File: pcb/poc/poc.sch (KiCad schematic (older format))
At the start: 57 parts, among them J1 USB_B_Mini, J2 Right, J3 Left, J4 AVR-ISP-6, J5 Conn_02x08_Odd_Even, J6 Conn_02x06_Odd_Even, SW1 SW_Push, SW2 SW_Push_45deg, SW3 SW_Push_45deg, SW4 SW_Push_45deg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

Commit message: pcb: poc: Assign footprints
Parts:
- added SW10, SW11: SW_Push_45deg, Button_Switch_Keyboard:SW_Cherry_MX_1.00u_PCB, symbol Switch:SW_Push_45deg
- C1: footprint (none) -> Capacitor_Tantalum_SMD:CP_EIA-3216-18_Kemet-A_Pad1.58x1.35mm_HandSolder
- C2, C3, C4, C5, C6, C7, C8, C9: footprint (none) -> Capacitor_SMD:C_0805_2012Metric_Pad1.18x1.45mm_HandSolder
- D10, D4: footprint (none) -> LED_SMD:LED_0805_2012Metric_Pad1.15x1.40mm_HandSolder
- D11, D12, D13, D14, D2, D6, D7, D8, D9: footprint (none) -> Diode_SMD:D_SOD-123
- F1: footprint (none) -> Fuse:Fuse_0805_2012Metric_Pad1.15x1.40mm_HandSolder
- J5: footprint (none) -> Connector_PinHeader_2.54mm:PinHeader_2x08_P2.54mm_Vertical
- J6: footprint (none) -> Connector_PinHeader_2.54mm:PinHeader_2x06_P2.54mm_Vertical
- R1, R10, R11, R12, R13, R14, R15, R2, R3, R4, R5, R6, R7, R8, R9: footprint (none) -> Resistor_SMD:R_0805_2012Metric_Pad1.20x1.40mm_HandSolder
- SW1, SW2, SW3, SW4, SW5, SW6, SW7, SW8, SW9: footprint (none) -> Button_Switch_THT:SW_PUSH_6mm_H4.3mm
- Y1: footprint (none) -> Crystal:Crystal_HC49-U_Vertical
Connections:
- net COL1: now also SW10.1
- net COL4: now also SW11.1
- net at D8.2 (A), SW4.2: now also SW10.2
- net at D13.2 (A), SW8.2: now also SW11.2

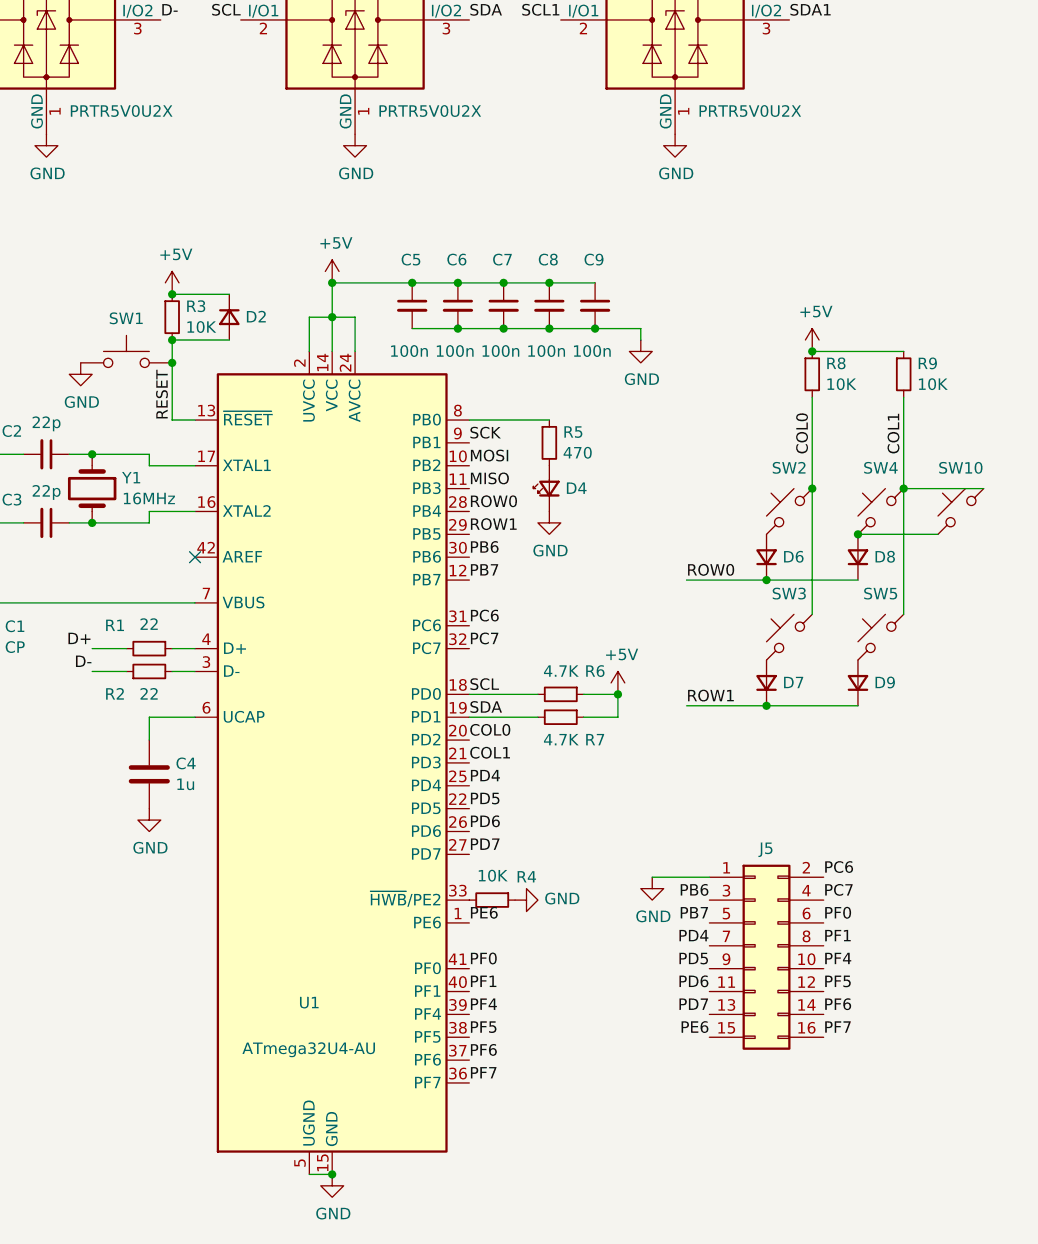
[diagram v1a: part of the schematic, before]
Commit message: pcb: poc: Some routing
Signed-off-by: Nikita Leshenko <nikita@leshenko.net>
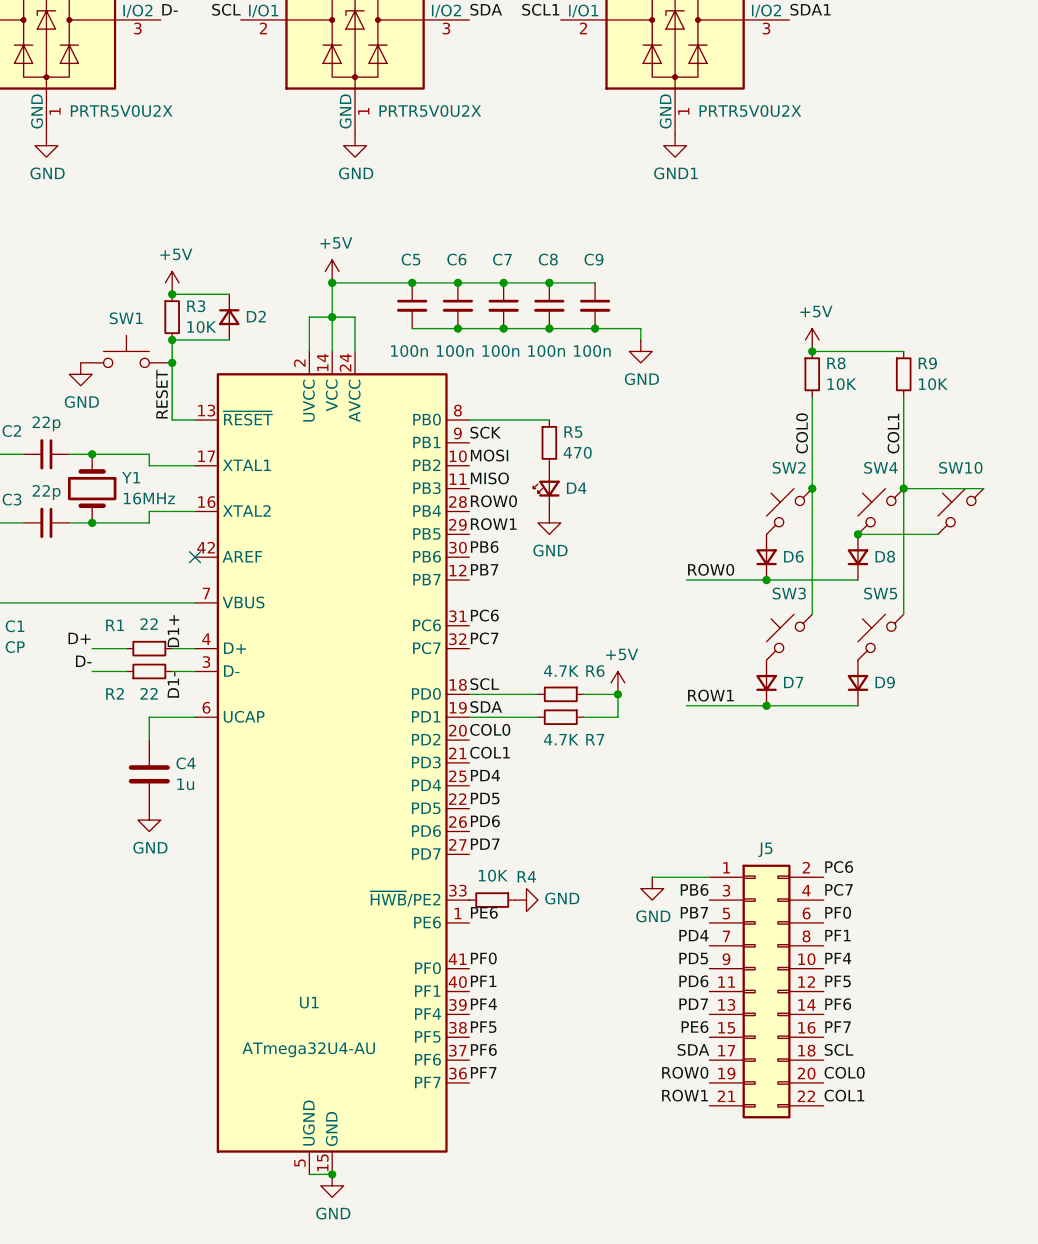
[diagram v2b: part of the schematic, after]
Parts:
- removed J5: Conn_02x08_Odd_Even, Connector_PinHeader_2.54mm:PinHeader_2x08_P2.54mm_Vertical, symbol Connector_Generic:Conn_02x08_Odd_Even
- added J5: Conn_02x11_Odd_Even, Connector_PinSocket_2.54mm:PinSocket_2x11_P2.54mm_Vertical, symbol Connector_Generic:Conn_02x11_Odd_Even
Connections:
- net COL0: now also J5.20 (Pin_20)
- net COL1: now also J5.22 (Pin_22)
- net GND: now also J5.1 (Pin_1); no longer D5.1 (GND)
- net GND1: now also D5.1 (GND)
- net PB6: now also J5.3 (Pin_3)
- net PB7: now also J5.5 (Pin_5)
- net PC6: now also J5.2 (Pin_2)
- net PC7: now also J5.4 (Pin_4)
- net PD4: now also J5.7 (Pin_7)
- net PD5: now also J5.9 (Pin_9)
- net PD6: now also J5.11 (Pin_11)
- net PD7: now also J5.13 (Pin_13)
- net PE6: now also J5.15 (Pin_15)
- net PF0: now also J5.6 (Pin_6)
- net PF1: now also J5.8 (Pin_8)
- net PF4: now also J5.10 (Pin_10)
- net PF5: now also J5.12 (Pin_12)
- net PF6: now also J5.14 (Pin_14)
- net PF7: now also J5.16 (Pin_16)
- net ROW0: now also J5.19 (Pin_19)
- net ROW1: now also J5.21 (Pin_21)
- net SCL: now also J5.18 (Pin_18)
- net SDA: now also J5.17 (Pin_17)
- net D1-: now reaches R2.2, U1.3 (D-)
- net D1+: now reaches R1.1, U1.4 (D+)
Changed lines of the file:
@@
-	1    0    0    -1
-$EndComp
-$Comp
-L power:GND #PWR027
-U 1 1 606CC318
-P 5150 1750
-F 0 "#PWR027" H 5150 1500 50  0001 C CNN
-F 1 "GND" H 5155 1577 50  0000 C CNN
-F 2 "" H 5150 1750 50  0001 C CNN
-F 3 "" H 5150 1750 50  0001 C CNN
-	1    5150 1750
 	1    0    0    -1
 $EndComp
@@
 Text Label 8650 4500 0    50   ~ 0
 COL4
-$Comp
-L Connector_Generic:Conn_02x08_Odd_Even J5
-U 1 1 60747A12
-P 5500 5300
-F 0 "J5" H 5550 5725 50  0000 C CNN
-F 1 "Conn_02x08_Odd_Even" H 5550 5726 50  0001 C CNN
-F 2 "Connector_PinHeader_2.54mm:PinHeader_2x08_P2.54mm_Vertical" H 5500 5300 50  0001 C CNN
-F 3 "~" H 5500 5300 50  0001 C CNN
-	1    5500 5300
-	1    0    0    -1
-$EndComp
 $Comp
 L Connector_Generic:Conn_02x06_Odd_Even J6
@@
 	10400 3500 10100 3500
 Connection ~ 10100 3500
+$Comp
+L power:GND1 #PWR0101
+U 1 1 604E5D44
+P 5150 1750
+F 0 "#PWR0101" H 5150 1500 50  0001 C CNN
+F 1 "GND1" H 5155 1577 50  0000 C CNN
+F 2 "" H 5150 1750 50  0001 C CNN
+F 3 "" H 5150 1750 50  0001 C CNN
+	1    5150 1750
+	1    0    0    -1
+$EndComp
+Text Label 5800 5800 0    50   ~ 0
+SCL
+Text Label 5300 5800 2    50   ~ 0
+SDA
+Text Label 5800 5900 0    50   ~ 0
+COL0
+Text Label 5800 6000 0    50   ~ 0
+COL1
+Text Label 5300 5900 2    50   ~ 0
+ROW0
+Text Label 5300 6000 2    50   ~ 0
+ROW1
+$Comp
+L Connector_Generic:Conn_02x11_Odd_Even J5
+U 1 1 604C9372
+P 5500 5500
+F 0 "J5" H 5550 6125 50  0000 C CNN
+F 1 "Conn_02x11_Odd_Even" H 5550 6126 50  0001 C CNN
+F 2 "Connector_PinSocket_2.54mm:PinSocket_2x11_P2.54mm_Vertical" H 5500 5500 50  0001 C CNN
+F 3 "~" H 5500 5500 50  0001 C CNN
+	1    5500 5500
+	1    0    0    -1
+$EndComp
+Text Label 3000 4000 1    50   ~ 0
+D1+
+Text Label 3000 4100 3    50   ~ 0
+D1-
 $EndSCHEMATC

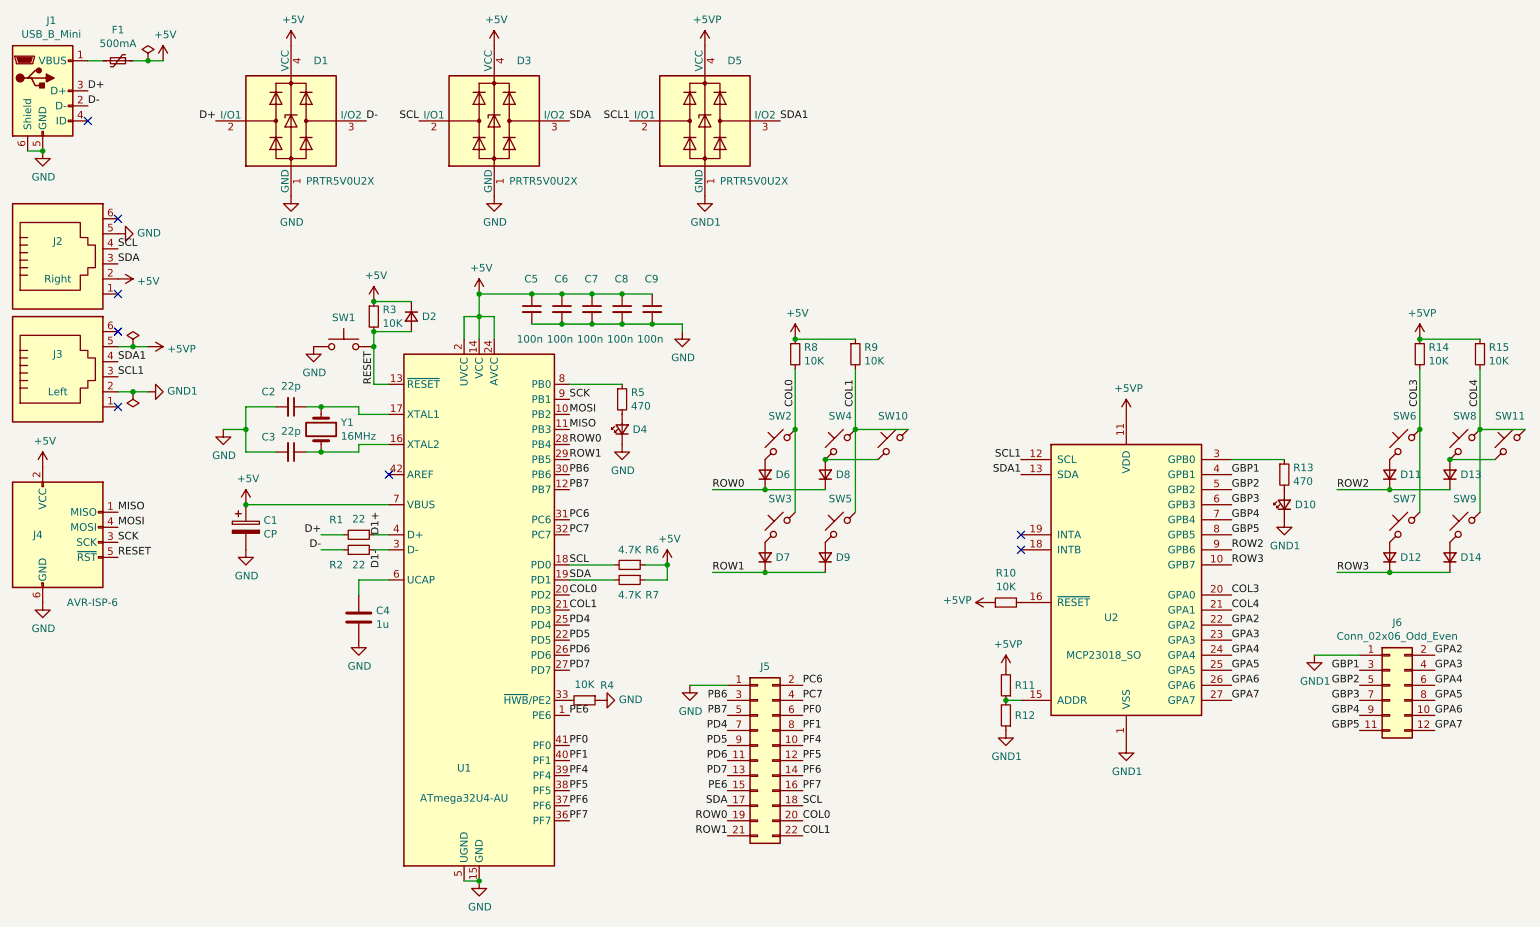
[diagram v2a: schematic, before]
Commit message: pcb: poc: Routed nabaz stuff
Signed-off-by: Nikita Leshenko <nikita@leshenko.net>
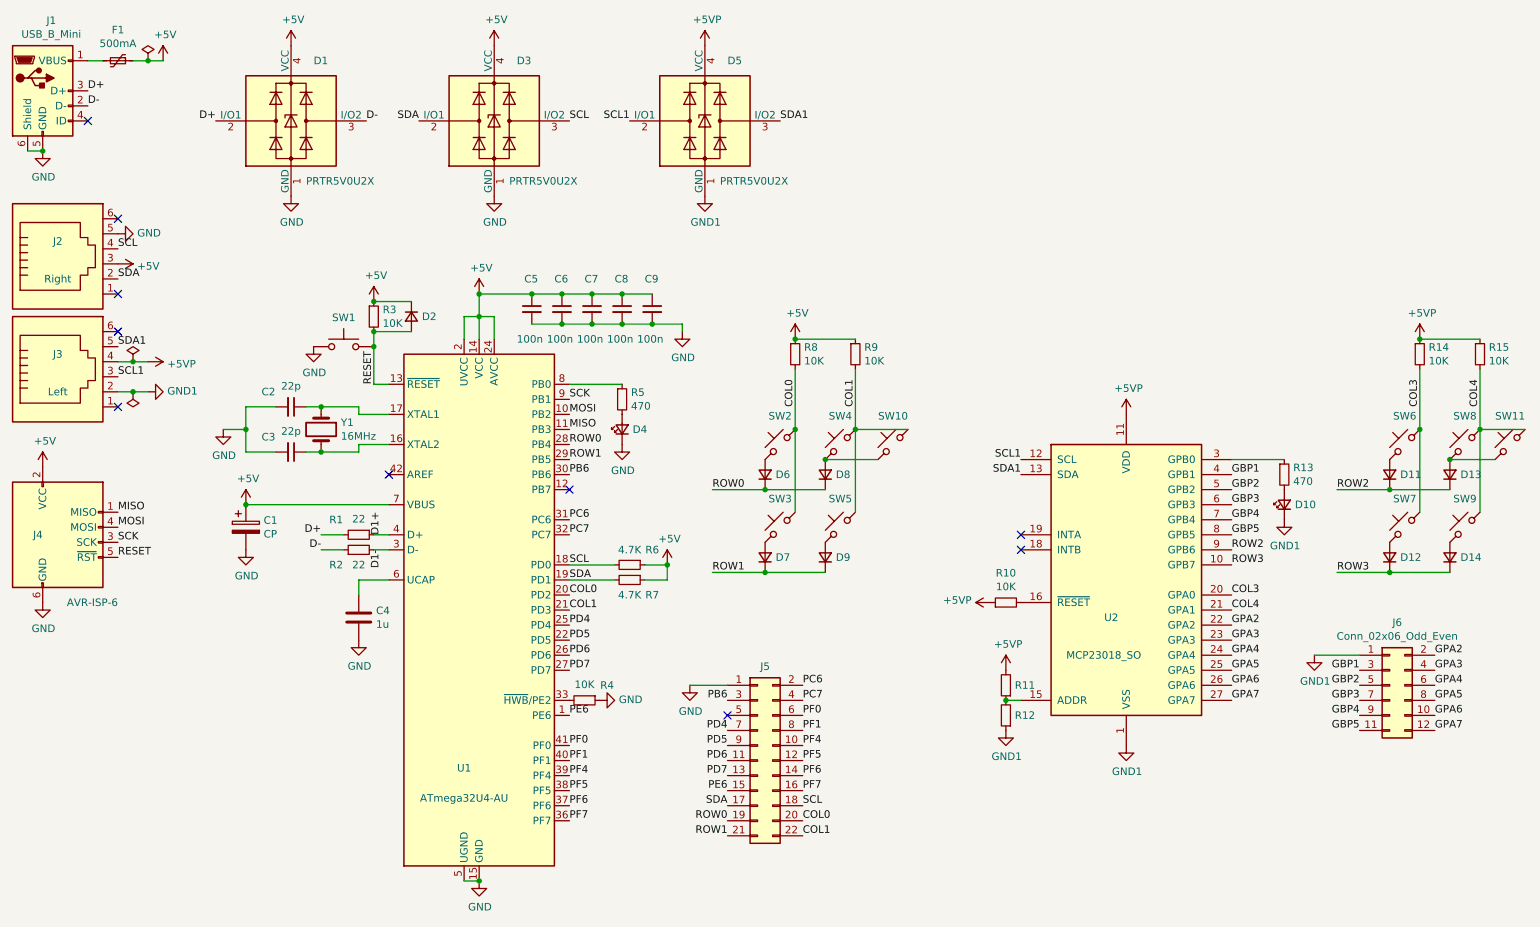
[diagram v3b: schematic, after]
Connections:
- net +5V: now also J2.3; no longer J2.2
- net +5VP: now also J3.4; no longer J3.5
- net SCL: now also D3.3 (I/O2); no longer D3.2 (I/O1)
- net SDA: now also D3.2 (I/O1), J2.2; no longer D3.3 (I/O2), J2.3
- net SDA1: now also J3.5; no longer J3.4
- net PB7: no longer names the net of U1.12 (PB7)
- net PB7: no longer J5.5 (Pin_5)
- no-connect marks 8 -> 10
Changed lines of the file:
@@
 L power:+5V #PWR05
 U 1 1 60464C52
-P 1250 2300
-F 0 "#PWR05" H 1250 2150 50  0001 C CNN
-F 1 "+5V" V 1265 2428 50  0000 L CNN
-F 2 "" H 1250 2300 50  0001 C CNN
-F 3 "" H 1250 2300 50  0001 C CNN
-	1    1250 2300
+P 1250 2200
+F 0 "#PWR05" H 1250 2050 50  0001 C CNN
+F 1 "+5V" V 1265 2328 50  0000 L CNN
+F 2 "" H 1250 2200 50  0001 C CNN
+F 3 "" H 1250 2200 50  0001 C CNN
+	1    1250 2200
 	0    1    1    0
 $EndComp
@@
 L power:+5VP #PWR06
 U 1 1 60466A48
-P 1450 2750
-F 0 "#PWR06" H 1450 2600 50  0001 C CNN
-F 1 "+5VP" V 1465 2878 50  0000 L CNN
-F 2 "" H 1450 2750 50  0001 C CNN
-F 3 "" H 1450 2750 50  0001 C CNN
-	1    1450 2750
+P 1450 2850
+F 0 "#PWR06" H 1450 2700 50  0001 C CNN
+F 1 "+5VP" V 1465 2978 50  0000 L CNN
+F 2 "" H 1450 2850 50  0001 C CNN
+F 3 "" H 1450 2850 50  0001 C CNN
+	1    1450 2850
 	0    1    1    0
 $EndComp
@@
 Text Label 1250 2100 0    50   ~ 0
 SCL
-Text Label 1250 2200 0    50   ~ 0
+Text Label 1250 2300 0    50   ~ 0
 SDA
-Text Label 1250 2850 0    50   ~ 0
+Text Label 1250 2750 0    50   ~ 0
 SDA1
 Text Label 1250 2950 0    50   ~ 0
@@
 Text Label 4250 3600 0    50   ~ 0
 PB6
-Text Label 4250 3700 0    50   ~ 0
-PB7
 Text Label 4250 3900 0    50   ~ 0
 PC6
@@
 Text Label 5800 5000 0    50   ~ 0
 PC6
-Text Label 5300 5200 2    50   ~ 0
-PB7
 Text Label 5300 5100 2    50   ~ 0
 PB6
@@
 	1    0    0    -1
 $EndComp
+Text Label 4250 1250 0    50   ~ 0
+SCL
 Text Label 3250 1250 2    50   ~ 0
-SCL
-Text Label 4250 1250 0    50   ~ 0
 SDA
 $Comp
@@
 L power:PWR_FLAG #FLG0101
 U 1 1 6079D7CB
-P 1350 2750
-F 0 "#FLG0101" H 1350 2825 50  0001 C CNN
-F 1 "PWR_FLAG" H 1350 2923 50  0001 C CNN
-F 2 "" H 1350 2750 50  0001 C CNN
-F 3 "~" H 1350 2750 50  0001 C CNN
-	1    1350 2750
-	1    0    0    -1
-$EndComp
-Wire Wire Line
-	1250 2750 1350 2750
-Connection ~ 1350 2750
-Wire Wire Line
-	1350 2750 1450 2750
+P 1350 2850
+F 0 "#FLG0101" H 1350 2925 50  0001 C CNN
+F 1 "PWR_FLAG" H 1350 3023 50  0001 C CNN
+F 2 "" H 1350 2850 50  0001 C CNN
+F 3 "~" H 1350 2850 50  0001 C CNN
+	1    1350 2850
+	1    0    0    -1
+$EndComp
+Wire Wire Line
+	1250 2850 1350 2850
+Connection ~ 1350 2850
+Wire Wire Line
+	1350 2850 1450 2850
 $Comp
 L power:PWR_FLAG #FLG0102
@@
 Text Label 3000 4100 3    50   ~ 0
 D1-
+NoConn ~ 4250 3700
+NoConn ~ 5300 5200
 $EndSCHEMATC
